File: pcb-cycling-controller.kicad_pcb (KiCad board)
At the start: 4 copper layers, 54.6 x 40.6 mm, 93 parts, among them J1 Power, J2 USB, J3 PROG, J6 LED1, J7 LED2, J8 SENSOR, J9 OLED, Q1 SI2301CDS-T1-GE3-ES, Q2 SI2301CDS-T1-GE3-ES, SW1 SS12F44G4, SW2 BTN1, SW3 BTN2, U1 ESP32-S3-WROOM-1, U2 LMV321, U3 AMS1117-5.0, U4 MT3410LB, U5 74AHCT125, U6 AMS1117-5.0, U7 DS1307Z+, Y2 32.768 kHz

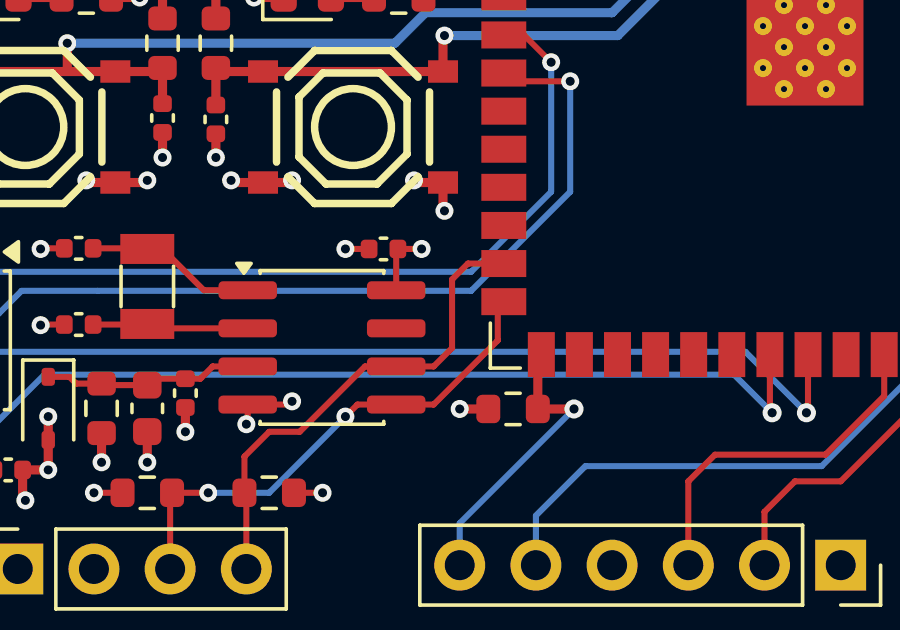
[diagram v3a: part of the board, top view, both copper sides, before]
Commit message: Update I2C pins due to #5
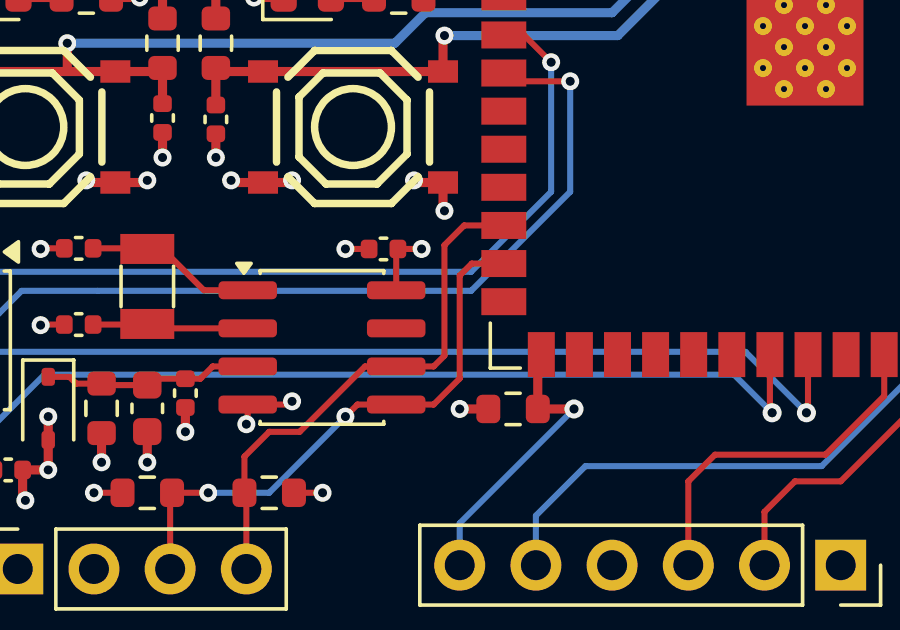
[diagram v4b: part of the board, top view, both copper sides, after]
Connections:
- U1 pad 24: unconnected-(U1-IO47-Pad24) -> I2C_SDA
- U1 pad 25: I2C_SDA -> I2C_SCL
- U1 pad 26: I2C_SCL -> unconnected-(U1-IO45-Pad26)
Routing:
- net I2C_SCL: track 16.9 -> 18.8 mm
- net I2C_SDA: track 16.4 -> 17.8 mm
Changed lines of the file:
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@@
 			(size 1.5 0.9)
 			(layers "F.Cu" "F.Mask" "F.Paste")
-			(net "unconnected-(U1-IO47-Pad24)")
+			(net "I2C_SDA")
 			(pinfunction "IO47_24")
 			(pintype "bidirectional")
@@
 			(size 1.5 0.9)
 			(layers "F.Cu" "F.Mask" "F.Paste")
-			(net "I2C_SDA")
+			(net "I2C_SCL")
 			(pinfunction "IO48_25")
 			(pintype "bidirectional")
@@
 			(size 1.5 0.9)
 			(layers "F.Cu" "F.Mask" "F.Paste")
-			(net "I2C_SCL")
+			(net "unconnected-(U1-IO45-Pad26)")
 			(pinfunction "IO45_26")
 			(pintype "bidirectional")
@@
 	)
 	(segment
-		(start 92.456 98.044)
-		(end 92.456 95.758)
+		(start 92.202 98.298)
+		(end 92.202 94.615)
 		(width 0.2032)
 		(layer "F.Cu")
@@
 	(segment
 		(start 91.841 98.659)
-		(end 92.456 98.044)
+		(end 92.202 98.298)
 		(width 0.2032)
 		(layer "F.Cu")
@@
 	)
 	(segment
-		(start 92.456 95.758)
-		(end 92.985 95.229)
+		(start 86.36 100.838)
+		(end 87.376 100.838)
 		(width 0.2032)
 		(layer "F.Cu")
@@
 	)
 	(segment
-		(start 86.36 100.838)
-		(end 87.376 100.838)
+		(start 92.202 94.615)
+		(end 92.858 93.959)
+		(width 0.2032)
+		(layer "F.Cu")
+		(net "I2C_SDA")
+	)
+	(segment
+		(start 90.593 98.659)
+		(end 91.841 98.659)
 		(width 0.2032)
 		(layer "F.Cu")
@@
 	)
 	(segment
-		(start 89.555 98.659)
-		(end 90.593 98.659)
+		(start 92.858 93.959)
+		(end 94.18 93.959)
 		(width 0.2032)
 		(layer "F.Cu")
@@
 	)
 	(segment
-		(start 90.593 98.659)
-		(end 91.841 98.659)
+		(start 89.555 98.659)
+		(end 90.593 98.659)
 		(width 0.2032)
 		(layer "F.Cu")
@@
 	)
 	(segment
-		(start 92.985 95.229)
-		(end 94.18 95.229)
-		(width 0.2032)
-		(layer "F.Cu")
-		(net "I2C_SDA")
-	)
-	(segment
 		(start 73.914 76.482)
 		(end 73.914 75.692)
@@
 	)
 	(segment
-		(start 91.841 99.929)
+		(start 89.301 99.929)
 		(end 90.593 99.929)
 		(width 0.2032)
@@
 	)
 	(segment
-		(start 89.301 99.929)
-		(end 90.593 99.929)
+		(start 92.71 99.06)
+		(end 92.71 95.631)
 		(width 0.2032)
 		(layer "F.Cu")
@@
 	)
 	(segment
-		(start 93.98 96.699)
-		(end 93.98 97.79)
+		(start 93.112 95.229)
+		(end 94.18 95.229)
 		(width 0.2032)
 		(layer "F.Cu")
@@
 	)
 	(segment
+		(start 92.71 95.631)
+		(end 93.112 95.229)
+		(width 0.2032)
+		(layer "F.Cu")
+		(net "I2C_SCL")
+	)
+	(segment
 		(start 83.058 105.41)
 		(end 83.058 102.933)
@@
 	)
 	(segment
-		(start 94.18 96.499)
-		(end 93.98 96.699)
+		(start 91.841 99.929)
+		(end 92.71 99.06)
 		(width 0.2032)
 		(layer "F.Cu")
@@
 	)
 	(segment
-		(start 93.98 97.79)
+		(start 90.593 99.929)
 		(end 91.841 99.929)
 		(width 0.2032)
@@
 		(net "Net-(U6-VO)")
 	)
+	(segment
+		(start 94.18 96.499)
+		(end 93.98 96.699)
+		(width 0.2032)
+		(layer "F.Cu")
+		(net "unconnected-(U1-IO45-Pad26)")
+	)
 	(zone

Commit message: Release candidate draft
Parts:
- removed C9: 1uF, Capacitor_SMD:C_0603_1608Metric
- removed R38, R39, R40: 0, Resistor_SMD:R_0603_1608Metric
- added C32: 0.1uF, Capacitor_SMD:C_0402_1005Metric, F.Cu at (90.3, 90.4)
- added C37: 0.1uF, Capacitor_SMD:C_0402_1005Metric, F.Cu at (88.6, 87.7)
- added C38: 22nF, Capacitor_SMD:C_0603_1608Metric, F.Cu at (86.6, 81.3)
- added H3: MountingHole, MountingHole:MountingHole_2.2mm_M2_ISO7380_Pad, F.Cu at (111.3, 112.0)
- added H4: MountingHole, MountingHole:MountingHole_2.2mm_M2_ISO7380_Pad, F.Cu at (68.8, 69.6)
- added J10: Sensor 1, Connector_Molex:Molex_KK-254_AE-6410-03A_1x03_P2.54mm_Vertical, F.Cu at (63.2, 89.2)
- added R14: 11k, Resistor_SMD:R_0603_1608Metric, F.Cu at (82.0, 88.6)
- added R32: 10k, Resistor_SMD:R_0603_1608Metric, F.Cu at (80.4, 88.6)
- added R33: 10k, Resistor_SMD:R_0603_1608Metric, F.Cu at (85.1, 90.8)
- added R37: 3.3k, Resistor_SMD:R_0603_1608Metric, F.Cu at (88.1, 90.8)
- added U8: LMV321, Package_TO_SOT_SMD:SOT-23-5_HandSoldering, F.Cu at (85.6, 88.2)
- C33: value 22uF 10V -> 0.1uF; footprint Capacitor_SMD:C_0603_1608Metric -> Capacitor_SMD:C_0402_1005Metric; moved to F.Cu
- C34: moved to F.Cu
- FID1, FID2, FID3: footprint Fiducial:Fiducial_1mm_Mask3mm -> Fiducial:Fiducial_1mm_Mask2mm
- J8: value SENSOR -> Sensor 1
- SW1: footprint mpn_footprints:SS12F44G4 -> MPN:SS12F44G4
- U1: value ESP32-S3-WROOM-1 -> ESP32-S3-WROOM-1-N8
- U4: value MT3410LB -> TX4113; footprint Package_TO_SOT_SMD:SOT-23-5 -> Package_TO_SOT_SMD:SOT-23-6
- U6: value AMS1117-5.0 -> BMI260; footprint Package_TO_SOT_SMD:SOT-223-3_TabPin2 -> Package_LGA:Bosch_LGA-14_3x2.5mm_P0.5mm; moved to F.Cu
- moved U6 32.3 mm to (97.3, 106.3), turned to 90 degrees
- moved C34 32.3 mm to (99.8, 107.4), turned to -90 degrees
- moved C33 29.6 mm to (97.6, 103.6), turned to 180 degrees
- moved C5 16.3 mm to (74.9, 82.3)
- moved R10 16.3 mm to (74.9, 79.3)
- moved R11 16.3 mm to (74.9, 80.8)
- moved D8 12.7 mm to (88.5, 75.0), turned to 0 degrees
- moved C20 10.7 mm to (79.7, 85.2), turned to 0 degrees
- moved R13 10.2 mm to (70.6, 85.9), turned to -90 degrees
- moved C31 9.10 mm to (76.9, 85.6), turned to -90 degrees
- moved R21 8.19 mm to (76.4, 88.7)
- moved R31 8.19 mm to (73.3, 88.7)
- moved U2 8.19 mm to (73.8, 86.1)
- moved H1 7.88 mm to (68.8, 112.0)
- moved C30 7.62 mm to (78.5, 88.2), turned to 90 degrees
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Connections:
- net SENSOR_FILT renamed SENSOR1_FILT
- C14 pad 2: Net-(U3-VO) -> VLED
- C15 pad 1: Net-(U3-VO) -> VLED
- C33 pad 1: GND -> +3V3
- C33 pad 2: Net-(U6-VO) -> GND
- C34 pad 1: Net-(U6-VO) -> +3V3
- J6 pad 1: VLED1 -> VLED
- J7 pad 1: VLED2 -> VLED
- U1 pad 4: unconnected-(U1-IO4-Pad4) -> SENSOR2_FILT
- U3 pad 2: Net-(U3-VO) -> VLED
- U4 pad 1: BUCK_VIN -> Net-(U4-BS)
- U4 pad 3: Net-(U4-SW) -> /BUCK_FB
- U4 pad 5: /BUCK_FB -> BUCK_VIN
- U6 pad 2: Net-(U6-VO) -> unconnected-(U6-ASDx-Pad2)
- U6 pad 3: VBAT_SW -> unconnected-(U6-ASCx-Pad3)
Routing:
- net VLED: track 1.50 -> 43.0 mm
- net SENSOR2_FILT: track 0.00 -> 26.1 mm, vias 0 -> 2
- net Net-(J10-Pin_2): track 0.00 -> 19.2 mm, vias 0 -> 1
- net BATT_VOLTAGE: track 20.1 -> 37.9 mm
- net I2C_SDA: track 17.8 -> 35.2 mm, vias 0 -> 2
- net VLED2: track 15.4 -> 0.00 mm, vias 2 -> 0
- net Net-(D8-A): track 30.3 -> 15.8 mm, vias 3 -> 2
- net VBAT_PROT: track 54.8 -> 68.6 mm, vias 1 -> 2
- net VBAT_SW: track 40.0 -> 26.4 mm, vias 7 -> 0
- net +3V3: track 28.1 -> 40.7 mm, vias 19 -> 20
- net Net-(U3-VO): track 12.1 -> 0.00 mm
- net I2C_SCL: track 18.8 -> 30.5 mm, vias 2 -> 4
- net Net-(U6-VO): track 11.0 -> 0.00 mm
- net /BUCK_FB: track 15.3 -> 5.64 mm, vias 2 -> 0
- net GND: track 73.2 -> 80.4 mm, vias 68 -> 78
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- added copper zone on In1.Cu, net GND
- removed copper zone on In2.Cu, net VBAT_SW
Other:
- board size 54.6 x 40.6 mm -> 54.6 x 47 mm
- board text added: "+"
- board text added: "-"
- board text added: "1"
- board text added: "2"
- board text added: "3.3V"
- board text added: "BATT"
- board text added: "C"
- board text added: "CYCLE CONTROLLER REV 1"
- board text added: "D"
- board text added: "FLASH"
- board text added: "G"
- board text added: "OFF"
- board text added: "ON"
- board text added: "RST"
- board text added: "RXD"
- board text added: "S"
- board text added: "SCL"
- board text added: "SDA"
- board text added: "SNS1"
- board text added: "SNS2"
- board text added: "STRIP1"
- board text added: "STRIP2"
- board text added: "TXD"
- board text added: "V"
- board text removed: "+12V"
- board text removed: "+5V"
- board text removed: "FIELD DEMO REV 1"
- board text removed: "RESET"
- board text removed: "S0"
- board text removed: "S1"
- board text removed: "S2"

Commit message: Fix +3.3V reg fb resistor values
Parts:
- R16: value 49.9k -> 100k
- R17: value 11k -> 22k
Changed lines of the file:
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@@
 			)
 		)
-		(property "Value" "11k"
+		(property "Value" "22k"
 			(at 0 1.43 0)
 			(layer "F.Fab")
@@
 			)
 		)
-		(property "Datasheet" "https://www.lcsc.com/datasheet/lcsc_datasheet_2206010045_UNI-ROYAL-Uniroyal-Elec-0603WAF1102T5E_C25950.pdf"
+		(property "Datasheet" ""
 			(at 0 0 0)
 			(layer "F.Fab")
@@
 			)
 		)
-		(property "LCSC Part #" "C25950"
+		(property "LCSC Part #" "C31850"
 			(at 0 0 180)
 			(unlocked yes)
@@
 			)
 		)
-		(property "Value" "49.9k"
+		(property "Value" "100k"
 			(at 0 1.43 90)
 			(layer "F.Fab")
@@
 			)
 		)
-		(property "Datasheet" "https://datasheet.lcsc.com/lcsc/2206010116_UNI-ROYAL-Uniroyal-Elec-0603WAF4992T5E_C23184.pdf"
+		(property "Datasheet" ""
 			(at 0 0 90)
 			(layer "F.Fab")
@@
 			)
 		)
-		(property "LCSC Part #" "C23184"
+		(property "LCSC Part #" "C25803"
 			(at 0 0 90)
 			(unlocked yes)

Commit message: Address design review feedback
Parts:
- added F1: 1.5A, Fuse:Fuse_1812_4532Metric, F.Cu at (70.3, 74.5)
- added SW4: FLASH, jlcpcb:SW-SMD_4P-L5.1-W5.1-P3.70-LS6.5-TL_H1.5, F.Cu at (98.0, 106.0)
- added SW5: RESET, jlcpcb:SW-SMD_4P-L5.1-W5.1-P3.70-LS6.5-TL_H1.5, F.Cu at (105.4, 106.0)
- J1: footprint Connector_Molex:Molex_KK-254_AE-6410-02A_1x02_P2.54mm_Vertical -> jlcpcb:CONN-TH_KF2510-2AW
- J10: value Sensor 1 -> Sensor 2; footprint Connector_Molex:Molex_KK-254_AE-6410-03A_1x03_P2.54mm_Vertical -> jlcpcb:CONN-TH_KF2510-3AW
- J6, J7: footprint Connector_Molex:Molex_KK-254_AE-6410-04A_1x04_P2.54mm_Vertical -> jlcpcb:CONN-TH_KF2510-4AW
- J8: footprint Connector_Molex:Molex_KK-254_AE-6410-03A_1x03_P2.54mm_Vertical -> jlcpcb:CONN-TH_KF2510-3AW
- R10: value 11k -> 22k
- R19: value 200 -> 1k
- moved C34 11.1 mm to (89.5, 111.6), turned to 180 degrees
- moved U6 7.23 mm to (90.7, 109.1), turned to 0 degrees
- moved C33 6.83 mm to (93.4, 108.9), turned to 90 degrees
- moved D1 6.69 mm to (69.3, 82.9), turned to 0 degrees
- moved Q2 6.67 mm to (68.2, 78.6), turned to 180 degrees
- moved Q1 5.79 mm to (72.2, 78.6), turned to 0 degrees
- moved R20 3.45 mm to (69.0, 85.9), turned to 90 degrees
- moved J6 3.40 mm to (64.8, 97.3), turned to -90 degrees
- moved R10 3.35 mm to (75.9, 82.5), turned to -90 degrees
- moved J7 3.18 mm to (64.8, 108.7), turned to -90 degrees
- moved D2 3.06 mm to (75.9, 78.4)
- moved J8 2.75 mm to (64.8, 78.2), turned to -90 degrees
- moved J10 2.54 mm to (64.8, 87.1), turned to -90 degrees
- moved J1 1.92 mm to (64.8, 70.6), turned to -90 degrees
- moved C5 1.61 mm to (73.6, 83.3)
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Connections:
- J1 pad 1: VBAT -> Net-(J1-Pin_1)
- R27 pad 2: Net-(J6-Pin_2) -> Net-(J6-Pin_3)
- R28 pad 2: Net-(J6-Pin_3) -> Net-(J6-Pin_2)
- R29 pad 2: Net-(J7-Pin_2) -> Net-(J7-Pin_3)
- R30 pad 2: Net-(J7-Pin_3) -> Net-(J7-Pin_2)
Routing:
- net Net-(Q2-G): track 1.87 -> 12.0 mm, vias 0 -> 2
- net GND: track 80.4 -> 88.3 mm, vias 78 -> 124
- net Net-(J1-Pin_1): track 0.00 -> 7.22 mm
- net I2C_SDA: track 35.2 -> 28.8 mm
- net ~{RST}: track 48.4 -> 42.7 mm, vias 1 -> 2
- net Net-(J6-Pin_3): track 12.5 -> 9.12 mm
- net BUCK_VIN: track 21.2 -> 24.4 mm
- net Net-(J8-Pin_2): track 9.60 -> 12.4 mm
- net Net-(J6-Pin_2): track 11.7 -> 9.69 mm
- net VBAT_SW: track 26.4 -> 24.4 mm
- net I2C_SCL: track 30.5 -> 28.6 mm
- net Net-(J10-Pin_2): track 19.2 -> 17.5 mm
- net VBAT_PROT: track 68.6 -> 67.1 mm, vias 2 -> 3
- net Net-(J7-Pin_2): track 7.36 -> 5.84 mm
- net VLED: track 43.0 -> 44.4 mm
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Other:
- board size 54.6 x 47 mm -> 52.8 x 47 mm
- board text added: "F"
- board text added: "R"
